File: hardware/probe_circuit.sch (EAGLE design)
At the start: 15 parts, among them J1 VPD, J2 VSIG, J3 VLED, J4 VOFF, J5 VPD, J6 VSIG, J7 VCC_IN, U1 LT1920CS8PBF

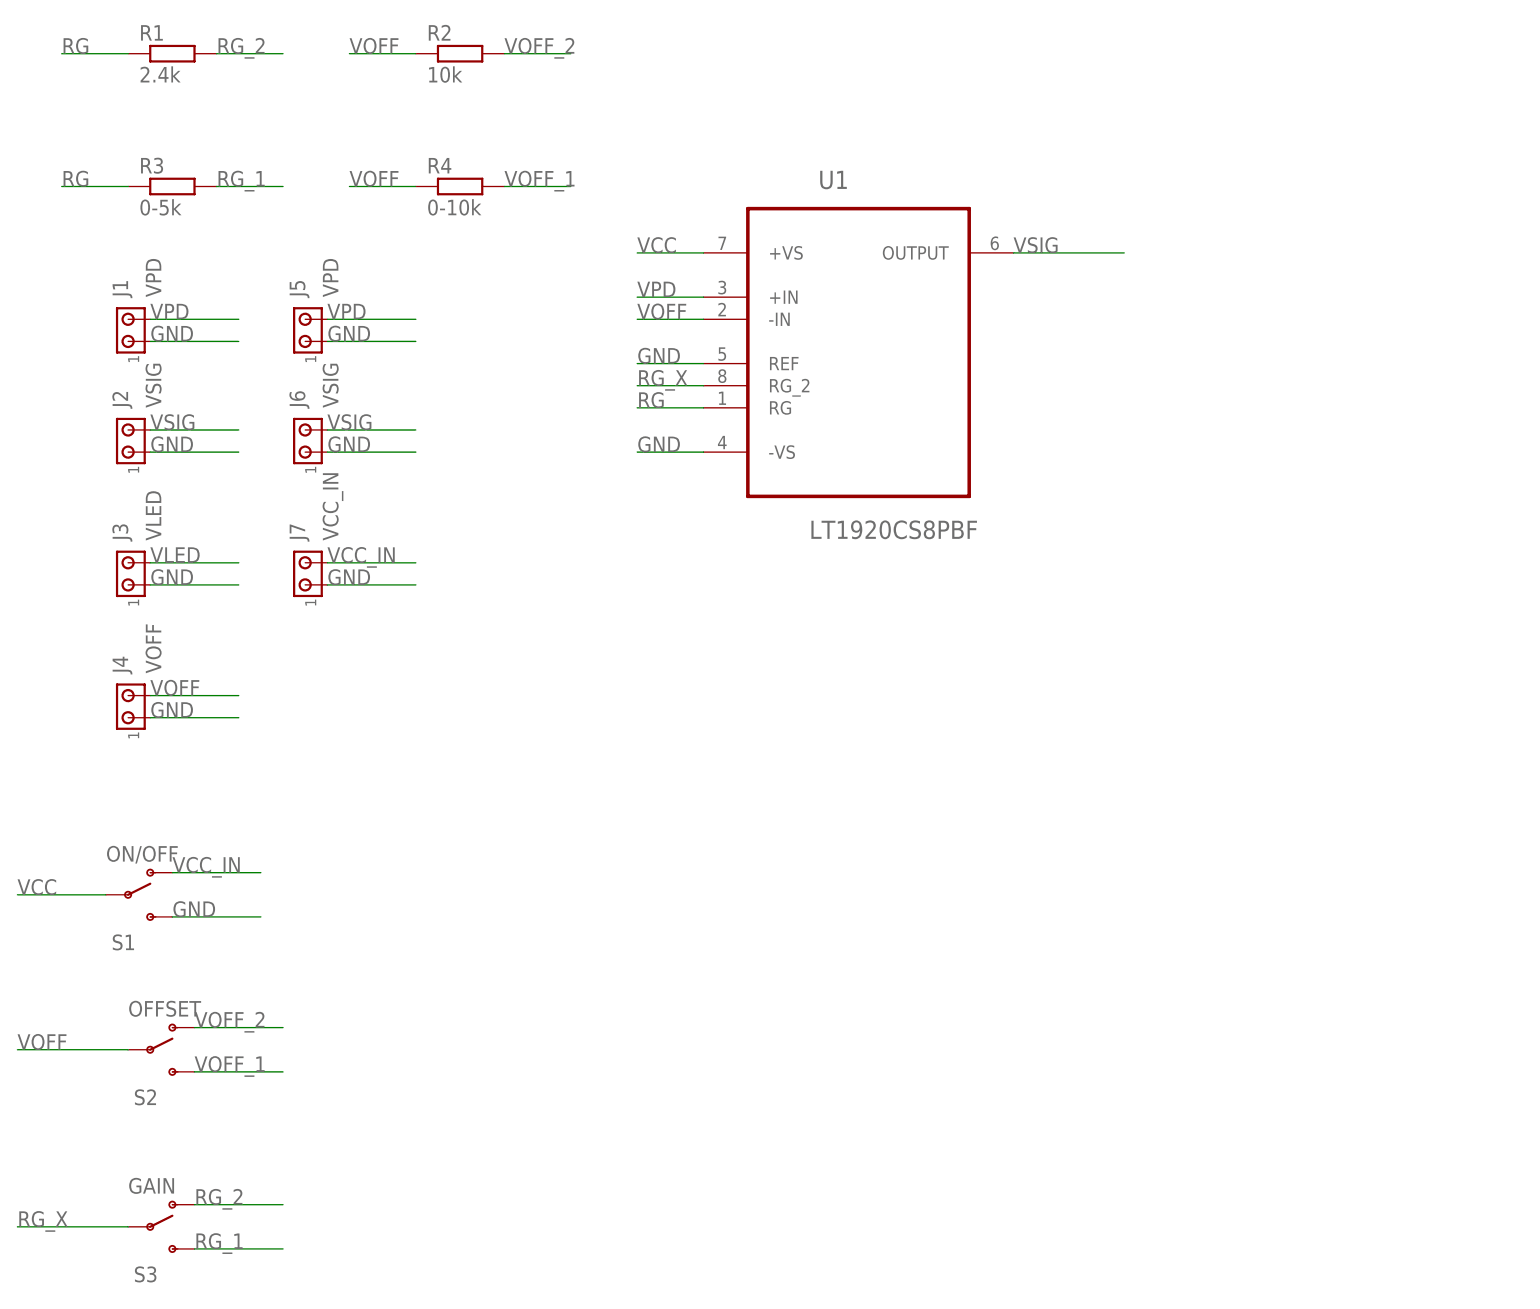
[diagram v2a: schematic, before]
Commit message: Added connectors for variable resisotrs and conmpressed board.
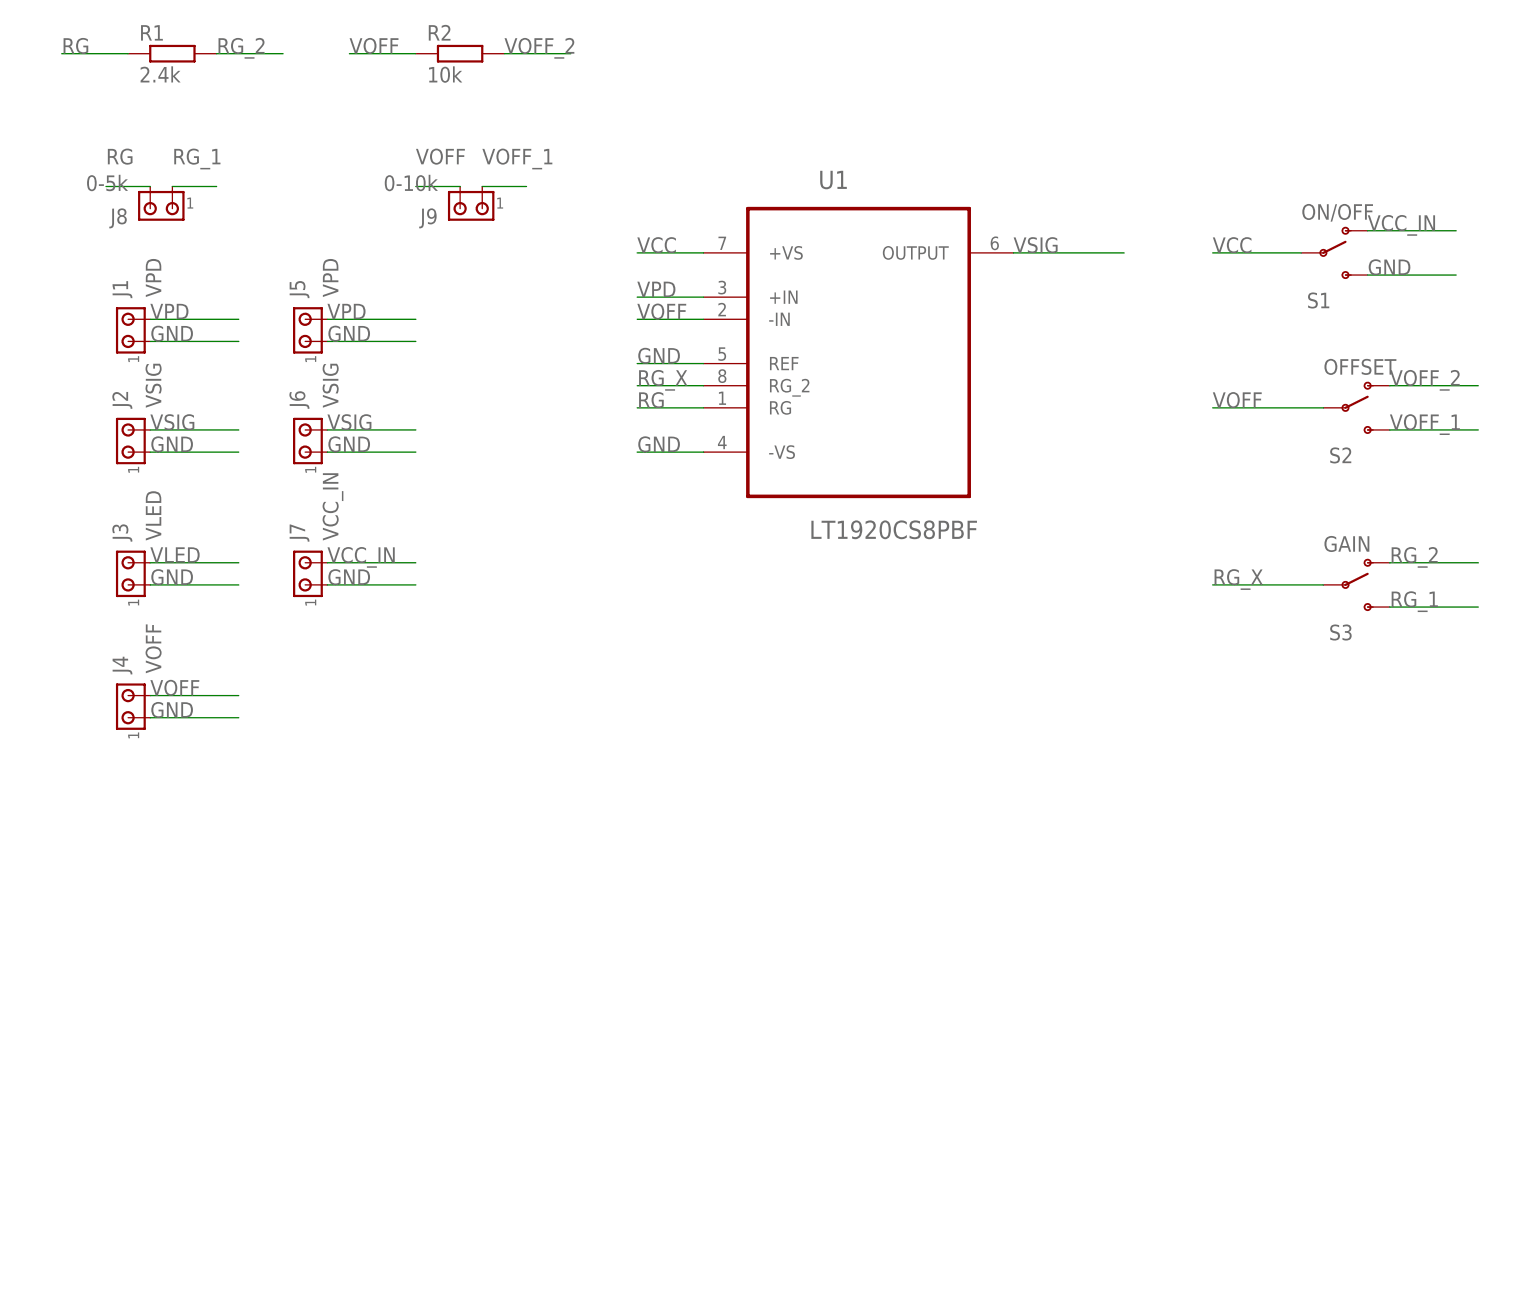
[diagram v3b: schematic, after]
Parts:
- removed R3: 0-5k, eagle-ltspice:R0204/7
- removed R4: 0-10k, eagle-ltspice:R0204/7
- added J8: 0-5k, con-amp:MTA02-100
- added J9: 0-10k, con-amp:MTA02-100
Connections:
- net RG: now also J8.2; no longer R3.1
- net RG_1: now also J8.1; no longer R3.2
- net VOFF: now also J9.2; no longer R4.1
- net VOFF_1: now also J9.1; no longer R4.2
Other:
- moved on the sheet: S1, S2, S3
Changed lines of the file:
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@@
 <setting verticaltext="up"/>
 </settings>
-<grid distance="0.1" unitdist="inch" unit="inch" style="lines" multiple="1" display="yes" altdistance="0.01" altunitdist="inch" altunit="inch"/>
+<grid distance="0.1" unitdist="inch" unit="inch" style="lines" multiple="1" display="no" altdistance="0.01" altunitdist="inch" altunit="inch"/>
 <layers>
 <layer number="1" name="Top" color="4" fill="1" visible="no" active="no"/>
@@
 <part name="S3" library="SparkFun-Electromechanical" deviceset="SWITCH-SPDT" device="PTH" value="GAIN"/>
 <part name="R2" library="eagle-ltspice" deviceset="R" device="0204/7" value="10k"/>
-<part name="R3" library="eagle-ltspice" deviceset="R" device="0204/7" value="0-5k"/>
-<part name="R4" library="eagle-ltspice" deviceset="R" device="0204/7" value="0-10k"/>
+<part name="J8" library="con-amp" deviceset="MTA02-100" device="" value="0-5k"/>
+<part name="J9" library="con-amp" deviceset="MTA02-100" device="" value="0-10k"/>
 </parts>
 <sheets>
@@
 <instance part="J5" gate="G$1" x="10.16" y="60.96" rot="R90"/>
 <instance part="J6" gate="G$1" x="10.16" y="48.26" rot="R90"/>
-<instance part="S1" gate="1" x="-10.16" y="-2.54"/>
+<instance part="S1" gate="1" x="127" y="71.12"/>
 <instance part="J7" gate="G$1" x="10.16" y="33.02" rot="R90"/>
-<instance part="S2" gate="1" x="-7.62" y="-20.32"/>
-<instance part="S3" gate="1" x="-7.62" y="-40.64"/>
+<instance part="S2" gate="1" x="129.54" y="53.34"/>
+<instance part="S3" gate="1" x="129.54" y="33.02"/>
 <instance part="R2" gate="G$1" x="27.94" y="93.98"/>
-<instance part="R3" gate="G$1" x="-5.08" y="78.74"/>
-<instance part="R4" gate="G$1" x="27.94" y="78.74"/>
+<instance part="J8" gate="G$1" x="-5.08" y="76.2" rot="R180"/>
+<instance part="J9" gate="G$1" x="30.48" y="76.2" rot="R180"/>
 </instances>
 <busses>
@@
 <segment>
 <pinref part="S3" gate="1" pin="O"/>
-<wire x1="7.62" y1="-38.1" x2="-2.54" y2="-38.1" width="0.1524" layer="91"/>
-<label x="-2.54" y="-38.1" size="1.778" layer="95"/>
+<wire x1="144.78" y1="35.56" x2="134.62" y2="35.56" width="0.1524" layer="91"/>
+<label x="134.62" y="35.56" size="1.778" layer="95"/>
 </segment>
 </net>
@@
 </segment>
 <segment>
-<pinref part="R3" gate="G$1" pin="1"/>
-<wire x1="-10.16" y1="78.74" x2="-17.78" y2="78.74" width="0.1524" layer="91"/>
-<label x="-17.78" y="78.74" size="1.778" layer="95"/>
+<wire x1="-12.7" y1="78.74" x2="-7.62" y2="78.74" width="0.1524" layer="91"/>
+<label x="-12.7" y="81.28" size="1.778" layer="95"/>
+<pinref part="J8" gate="G$1" pin="2"/>
 </segment>
 </net>
@@
 <segment>
 <pinref part="S1" gate="1" pin="P"/>
-<wire x1="-12.7" y1="-2.54" x2="-22.86" y2="-2.54" width="0.1524" layer="91"/>
-<label x="-22.86" y="-2.54" size="1.778" layer="95"/>
+<wire x1="124.46" y1="71.12" x2="114.3" y2="71.12" width="0.1524" layer="91"/>
+<label x="114.3" y="71.12" size="1.778" layer="95"/>
 </segment>
 </net>
@@
 <segment>
 <pinref part="S2" gate="1" pin="P"/>
-<wire x1="-10.16" y1="-20.32" x2="-22.86" y2="-20.32" width="0.1524" layer="91"/>
-<label x="-22.86" y="-20.32" size="1.778" layer="95"/>
+<wire x1="127" y1="53.34" x2="114.3" y2="53.34" width="0.1524" layer="91"/>
+<label x="114.3" y="53.34" size="1.778" layer="95"/>
 </segment>
 <segment>
@@
 </segment>
 <segment>
-<pinref part="R4" gate="G$1" pin="1"/>
-<wire x1="22.86" y1="78.74" x2="15.24" y2="78.74" width="0.1524" layer="91"/>
-<label x="15.24" y="78.74" size="1.778" layer="95"/>
+<wire x1="22.86" y1="78.74" x2="27.94" y2="78.74" width="0.1524" layer="91"/>
+<label x="22.86" y="81.28" size="1.778" layer="95"/>
+<pinref part="J9" gate="G$1" pin="2"/>
 </segment>
 </net>
@@
 <segment>
 <pinref part="S1" gate="1" pin="S"/>
-<wire x1="5.08" y1="-5.08" x2="-5.08" y2="-5.08" width="0.1524" layer="91"/>
-<label x="-5.08" y="-5.08" size="1.778" layer="95"/>
+<wire x1="142.24" y1="68.58" x2="132.08" y2="68.58" width="0.1524" layer="91"/>
+<label x="132.08" y="68.58" size="1.778" layer="95"/>
 </segment>
 <segment>
@@
 <segment>
 <pinref part="S1" gate="1" pin="O"/>
-<wire x1="-5.08" y1="0" x2="5.08" y2="0" width="0.1524" layer="91"/>
-<label x="-5.08" y="0" size="1.778" layer="95"/>
+<wire x1="132.08" y1="73.66" x2="142.24" y2="73.66" width="0.1524" layer="91"/>
+<label x="132.08" y="73.66" size="1.778" layer="95"/>
 </segment>
 <segment>
@@
 <segment>
 <pinref part="S3" gate="1" pin="P"/>
-<wire x1="-22.86" y1="-40.64" x2="-10.16" y2="-40.64" width="0.1524" layer="91"/>
-<label x="-22.86" y="-40.64" size="1.778" layer="95"/>
+<wire x1="114.3" y1="33.02" x2="127" y2="33.02" width="0.1524" layer="91"/>
+<label x="114.3" y="33.02" size="1.778" layer="95"/>
 </segment>
 <segment>
@@
 <segment>
 <pinref part="S3" gate="1" pin="S"/>
-<wire x1="-2.54" y1="-43.18" x2="7.62" y2="-43.18" width="0.1524" layer="91"/>
-<label x="-2.54" y="-43.18" size="1.778" layer="95"/>
-</segment>
-<segment>
-<pinref part="R3" gate="G$1" pin="2"/>
-<wire x1="0" y1="78.74" x2="7.62" y2="78.74" width="0.1524" layer="91"/>
-<label x="0" y="78.74" size="1.778" layer="95"/>
+<wire x1="134.62" y1="30.48" x2="144.78" y2="30.48" width="0.1524" layer="91"/>
+<label x="134.62" y="30.48" size="1.778" layer="95"/>
+</segment>
+<segment>
+<wire x1="0" y1="78.74" x2="-5.08" y2="78.74" width="0.1524" layer="91"/>
+<label x="-5.08" y="81.28" size="1.778" layer="95"/>
+<pinref part="J8" gate="G$1" pin="1"/>
 </segment>
 </net>
@@
 <segment>
 <pinref part="S2" gate="1" pin="S"/>
-<wire x1="-2.54" y1="-22.86" x2="7.62" y2="-22.86" width="0.1524" layer="91"/>
-<label x="-2.54" y="-22.86" size="1.778" layer="95"/>
-</segment>
-<segment>
-<pinref part="R4" gate="G$1" pin="2"/>
-<wire x1="33.02" y1="78.74" x2="40.64" y2="78.74" width="0.1524" layer="91"/>
-<label x="33.02" y="78.74" size="1.778" layer="95"/>
+<wire x1="134.62" y1="50.8" x2="144.78" y2="50.8" width="0.1524" layer="91"/>
+<label x="134.62" y="50.8" size="1.778" layer="95"/>
+</segment>
+<segment>
+<wire x1="35.56" y1="78.74" x2="30.48" y2="78.74" width="0.1524" layer="91"/>
+<label x="30.48" y="81.28" size="1.778" layer="95"/>
+<pinref part="J9" gate="G$1" pin="1"/>
 </segment>
 </net>
@@
 <segment>
 <pinref part="S2" gate="1" pin="O"/>
-<wire x1="7.62" y1="-17.78" x2="-2.54" y2="-17.78" width="0.1524" layer="91"/>
-<label x="-2.54" y="-17.78" size="1.778" layer="95"/>
-</segment>
-<segment>
+<wire x1="144.78" y1="55.88" x2="134.62" y2="55.88" width="0.1524" layer="91"/>
+<label x="134.62" y="55.88" size="1.778" layer="95"/>
+</segment>
+<segment>

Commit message: Printed brd and sch files to pdf
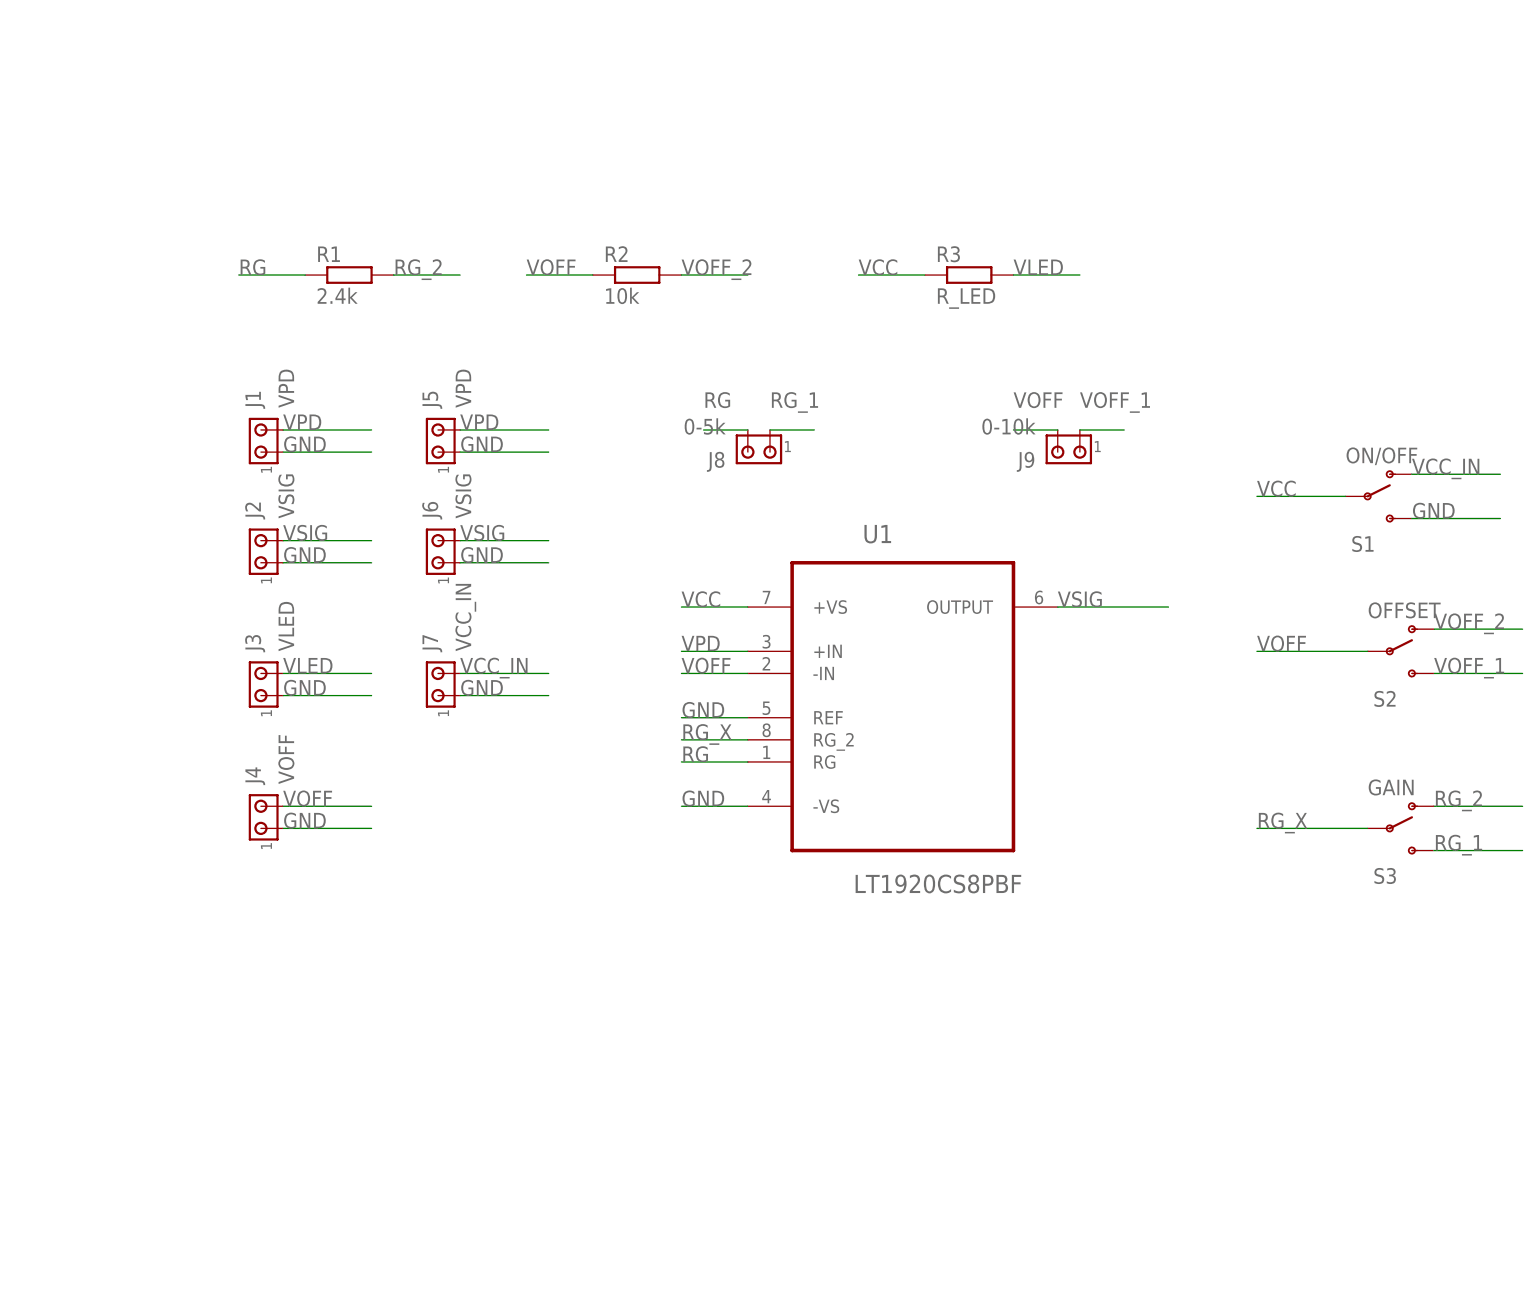
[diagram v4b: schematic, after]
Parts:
- added R3: R_LED, eagle-ltspice:R0204/7
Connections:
- net VCC: now also R3.1
- net VLED: now also R3.2
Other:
- moved on the sheet: J1, J2, J3, J4, J5, J6, J7, J8, J9, R1, R2, S1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
